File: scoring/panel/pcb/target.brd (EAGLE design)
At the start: 31.7 x 14.9 mm, 13 parts, among them J1 AVRISP6_COMPACT, U1 ATTINY85-20SU

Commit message: Panel PCB: Update the decoupling cap to be a 1uF one instead of 0.1uF.
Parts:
- C1: value .1uF -> 1uF
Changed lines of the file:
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@@
 <attribute name="PRICE10" value="1.386" x="13.97" y="6.604" size="1.778" layer="27" rot="R180" display="off"/>
 </element>
-<element name="C1" library="rcl" package="C0805" value=".1uF" x="14.605" y="11.049" smashed="yes">
+<element name="C1" library="rcl" package="C0805" value="1uF" x="14.605" y="11.049" smashed="yes">
 <attribute name="NAME" x="14.097" y="12.319" size="1.016" layer="25"/>
-<attribute name="DPN" value="399-1168-1-ND" x="14.605" y="11.049" size="1.778" layer="27" display="off"/>
-<attribute name="PRICE10" value="0.05" x="14.605" y="11.049" size="1.778" layer="27" display="off"/>
+<attribute name="DPN" value="399-8004-1-ND" x="14.605" y="11.049" size="1.778" layer="27" display="off"/>
+<attribute name="PRICE10" value="0.13" x="14.605" y="11.049" size="1.778" layer="27" display="off"/>
 </element>
 <element name="PWR" library="led" package="SML0805" value="" x="10.16" y="11.049" smashed="yes" rot="R270">

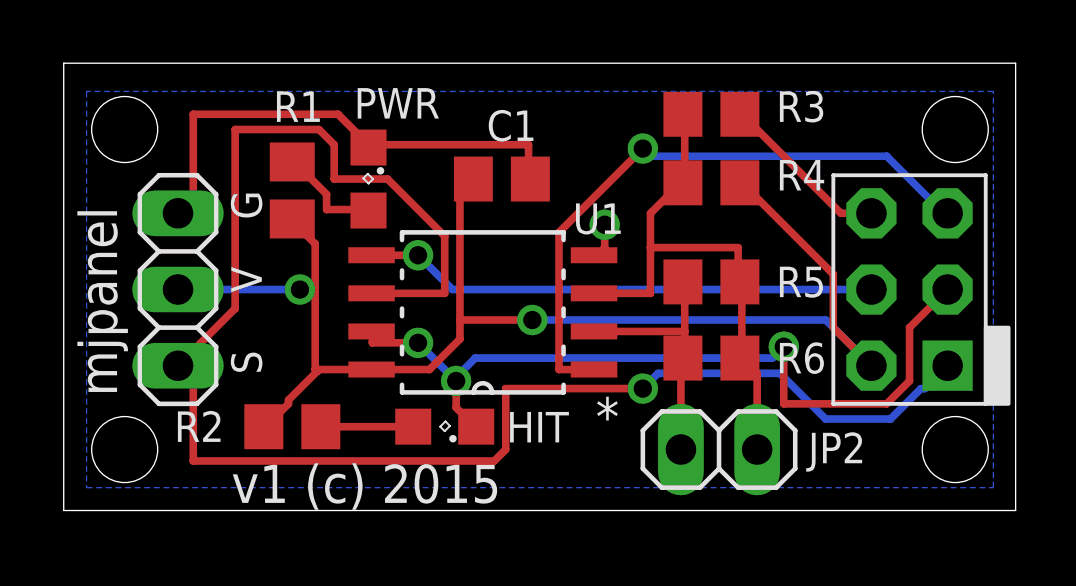
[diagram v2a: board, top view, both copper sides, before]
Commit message: Draft of scoring panel with mounting holes slightly closer to the edge, converted to use macrofab parts, with a JST connector, and a pullup on the signal line.
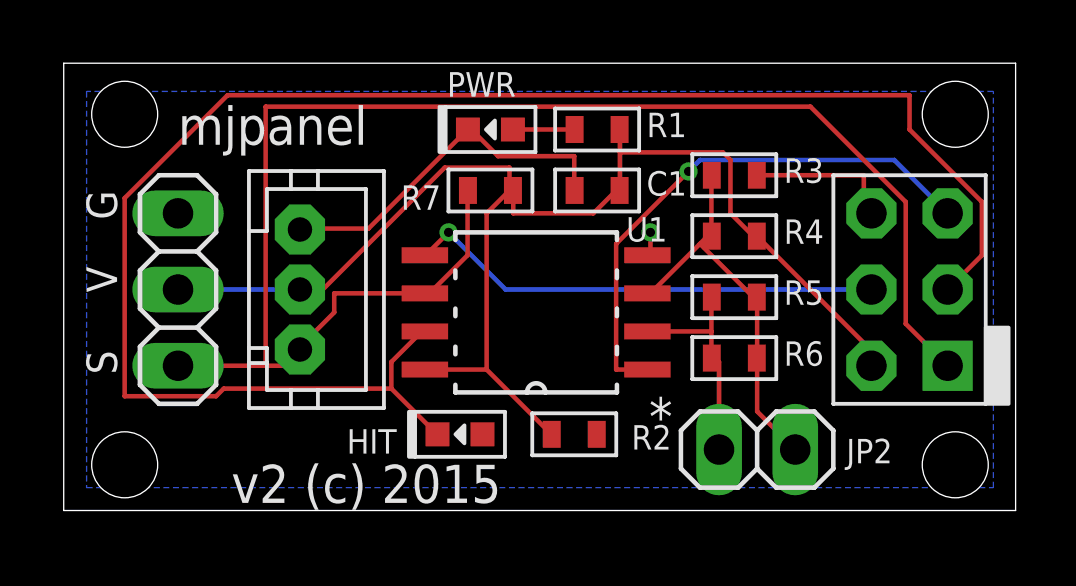
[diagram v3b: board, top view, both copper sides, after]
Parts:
- added R7: 2k, MF_Passives:R0603
- added U$1: JST-PH3, jst-ph:JST-PH3
- C1: device rcl:C0805 -> MF_Passives:C0603
- HIT: value (none) -> GRN; device led:SML0805 -> MF_LEDs:LED0603
- PWR: value (none) -> RED; device led:SML0805 -> MF_LEDs:LED0603
- R1, R2: value 680 -> 560; device rcl:R0805 -> MF_Passives:R0603
- R3, R4, R5, R6: device rcl:R0805 -> MF_Passives:R0603
- moved R1 10.4 mm to (17.8, 12.7), turned to 0 degrees
- moved R2 9.40 mm to (17.0, 2.54)
- moved PWR 4.39 mm to (14.2, 12.7), turned to 0 degrees
- moved C1 3.20 mm to (17.8, 10.7), turned to 180 degrees
- moved R3 2.17 mm to (22.4, 11.2)
- moved R4 1.93 mm to (22.4, 9.14)
- moved U1 1.78 mm to (15.7, 6.60)
- moved JP2 1.27 mm to (23.1, 2.03)
- moved R5 0.92 mm to (22.4, 7.11)
- moved R6 0.76 mm to (22.4, 5.08)
- moved HIT 0.57 mm to (13.2, 2.54), turned to 0 degrees
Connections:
- new net ANODE: HIT.ANODE
- net GND: now also C1.P$2, PWR.CATHODE, R3.P$1, U$1.3; no longer C1.2, PWR.C, R3.1
- net N$1: now also PWR.ANODE, R1.P$1; no longer PWR.A, R1.1
- net N$3: now also R3.P$2, R4.P$2, R5.P$1, R6.P$1; no longer R3.2, R4.2, R5.1, R6.1
- net N$4: now also HIT.CATHODE; no longer HIT.C
- net N$5: now also R2.P$1; no longer HIT.A, R2.1
- net N$6: now also R5.P$2, R6.P$2; no longer R5.2, R6.2
- net N$8: now also R7.P$1, U$1.1
- net VCC: now also C1.P$1, R1.P$2, R2.P$2, R4.P$1, R7.P$2, U$1.2; no longer C1.1, R1.2, R2.2, R4.1
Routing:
- net N$4: track 27.0 -> 55.7 mm, vias 3 -> 0
- net GND: track 23.4 -> 17.9 mm
- net N$3: track 18.5 -> 13.4 mm
- net N$8: track 55.2 -> 51.4 mm, vias 1 -> 0
- net N$5: track 3.08 -> 0.00 mm
- net N$2: track 20.7 -> 18.2 mm
- net N$1: track 3.62 -> 2.06 mm
- net N$6: track 8.80 -> 7.41 mm
- net VCC: track 45.7 -> 44.4 mm, vias 2 -> 0
- net N$7: track 17.1 -> 16.0 mm
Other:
- board text added: "v2 (c) 2015"
- board text removed: "v1 (c) 2015"

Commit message: Add resistor inline on signal line.  Run ERC and DRC.
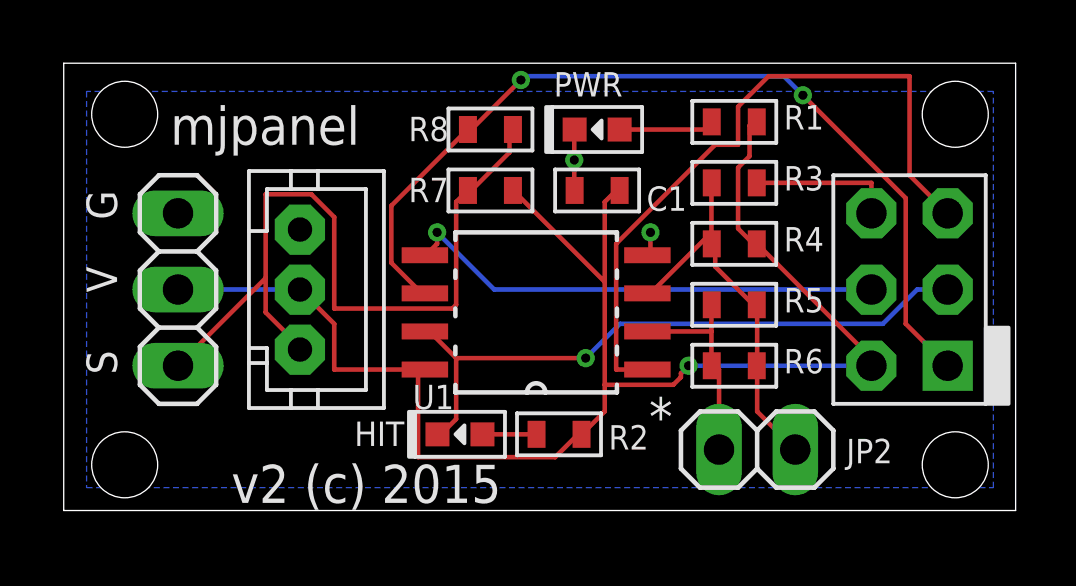
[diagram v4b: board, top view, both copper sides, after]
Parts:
- added R8: 47, MF_Passives:R0603
- moved R1 4.58 mm to (22.4, 13.0)
- moved PWR 3.56 mm to (17.8, 12.7)
- moved R2 0.51 mm to (16.5, 2.54), turned to 0 degrees
- moved R5 0.25 mm to (22.4, 6.86)
- moved R6 0.25 mm to (22.4, 4.83)
- moved R3 0.25 mm to (22.4, 10.9)
- moved R4 0.25 mm to (22.4, 8.89)
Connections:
- removed net ANODE: HIT.ANODE
- new net N$9: J1.1, R8.P$1, U1.6
- net N$5: now also HIT.ANODE
- net N$8: now also R8.P$2; no longer J1.1, U1.6
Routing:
- net N$4: track 55.7 -> 21.6 mm, vias 0 -> 1
- net N$9: track 0.00 -> 30.2 mm, vias 0 -> 2
- net N$8: track 51.4 -> 26.3 mm
- net GND: track 17.9 -> 7.76 mm, vias 1 -> 2
- net VCC: track 44.4 -> 51.7 mm, vias 0 -> 1
- net N$2: track 18.2 -> 23.2 mm, vias 1 -> 0
- net N$5: track 0.00 -> 1.80 mm
- net N$1: track 2.06 -> 3.33 mm
